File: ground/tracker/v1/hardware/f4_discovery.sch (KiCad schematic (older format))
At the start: 22 parts

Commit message: changed optimisation from Os to O3 and moved clearing of exti to just after it was read as set. Now seems to be not giving exti failed messages. So looks like its stable at the mo
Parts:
- removed C?: 0.1uF, symbol C
- removed D?: DIODE, symbol DIODE
- removed H-Bridge, P? (x2): CONN_1, symbol CONN_1
- removed P?: H-bridge GND, symbol CONN_1
- removed P?: CONN_4, symbol CONN_4
- added C1: 0.1uF, symbol C
- added C2: 1000uF, symbol CP1
- added C?: 100uF, symbol CP1
- added K2: CONN_3, symbol CONN_3
- added P2: CONN_6, symbol CONN_6
- added P5, P6, P? (x2): CONN_1, symbol CONN_1
- added P8: MAGGPS, symbol CONN_9
- added R1: 100R, symbol R
- added R10, R11, R12, R13, R14, R15, R16, R3, R4, R5, R6, R7, R8, R9: R, symbol R
- added R17, R2: 50R, symbol R
- added R? (x2): 10k, symbol R
- added SW?: SPST, symbol SPST
- added U3: BEC, symbol 7805
- added U?: 24C16, symbol 24C16
- C4: renamed from C?; value 470uF -> 10uF
- P9: renamed from P?; value CONN_5 -> RCOUT
- gave numbers to parts that had none: 13
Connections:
- net labels added: +12V, +3.3V, +6V, AV_TELEM_CDT, AV_TELEM_IN, AXMOTBV, AZ5V, AZMOT5V, AZMOTAV, AZMOTGND, AZNDIR, AZSENS, BEC5V, DiAZDIR, DiAZENCA, DiAZENCB, DiAZMOTAV, DiAZMOTBV, DiAZNDIR, DiAZPWM, DiGPSRXI, DiGPSTXO, DiMAGRDY, DiMAGSCL, DiMAGSDA, DiSLSPRXI, DiSLSPTXO, DiTSSIG, GPS5V, GPSGND, GPSRXI, GPSTXO, MAG5V, MAGGND, MAGRDY, MAGSCL, MAGSDA, RCGND, SLSPGND, SLSPRXI, SLSPTXO, TSBEC5V, TSGND, TSSIG
- net labels removed: 5VBEC, AZMOTA, AZMOTB, AZSENSE, ENC5V, ENCGND, NAZDIR, RCOUTGND, SP1RXI, SP1TXO, SPI1GND, TLTSRVOPWM
- wire segments 144 -> 329
- no-connect marks 0 -> 4
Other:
- moved on the sheet: C4, C5, C6, K1, P1, P10, P11, P12, P3, P4, P7, P9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

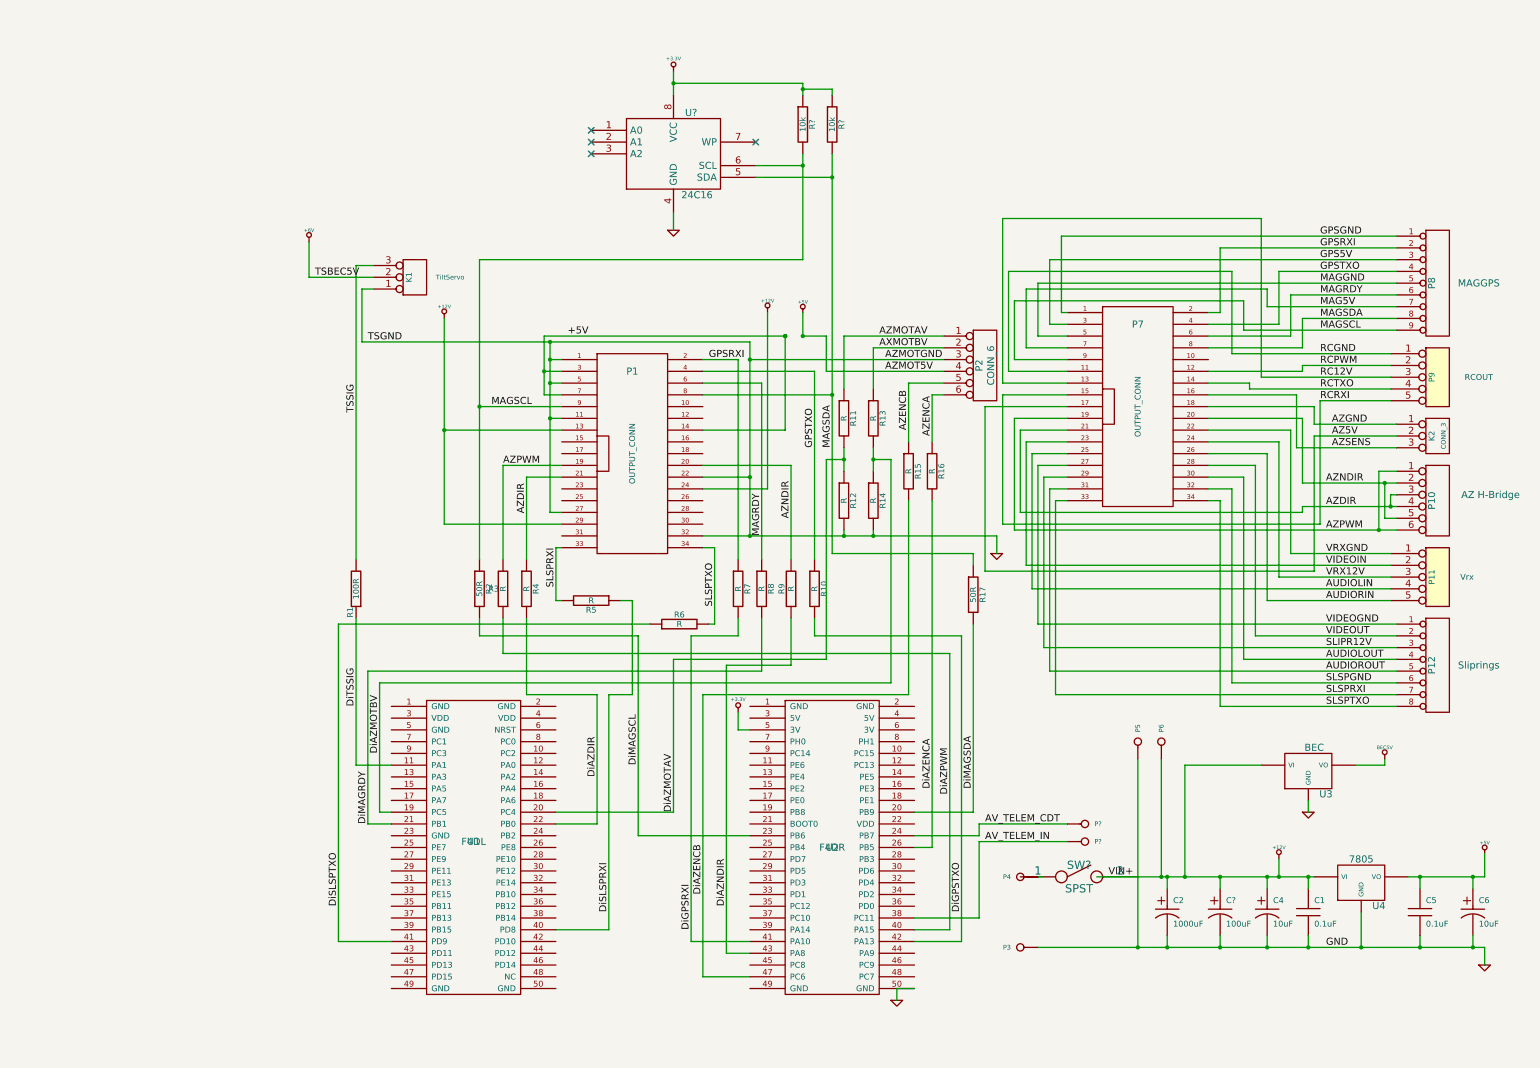
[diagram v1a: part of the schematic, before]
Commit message: prior to sorting serial port naming
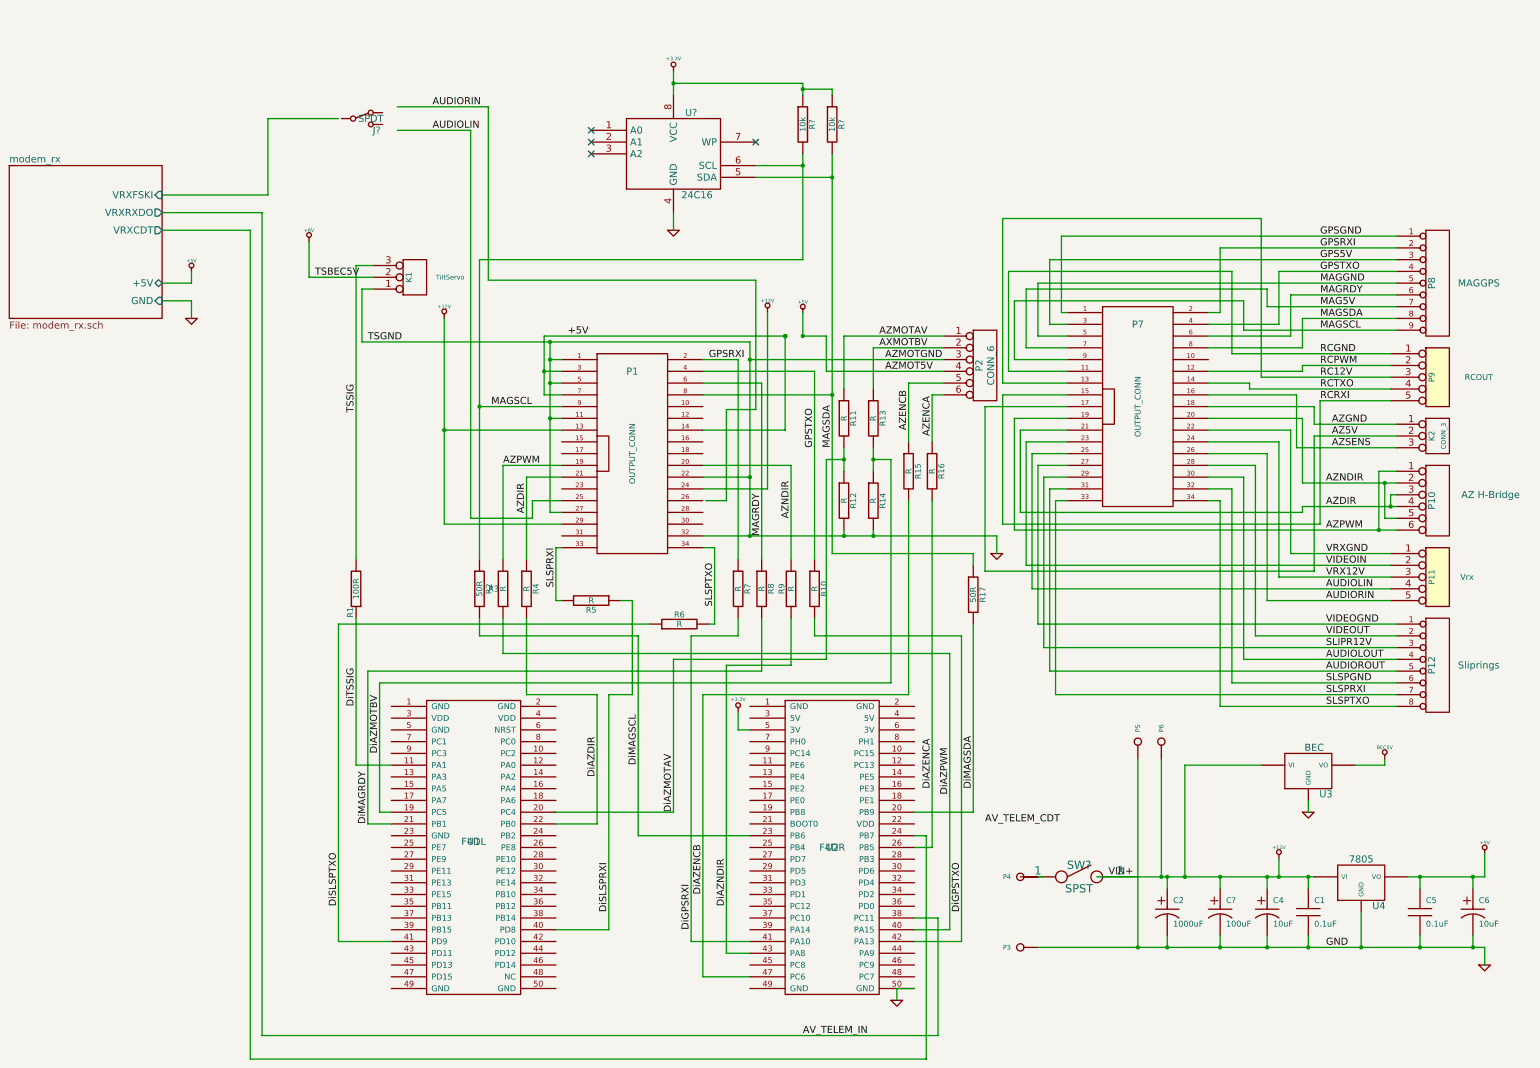
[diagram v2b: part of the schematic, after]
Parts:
- removed P? (x2): CONN_1, symbol CONN_1
- added J?: SPDT, symbol SPDT
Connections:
- net AUDIOLIN: now also P1.25 (P25)
- net AV_TELEM_CDT: no longer U2.24 (PB7)
- new net modem_rx/VRXCDT: U2.24 (PB7)

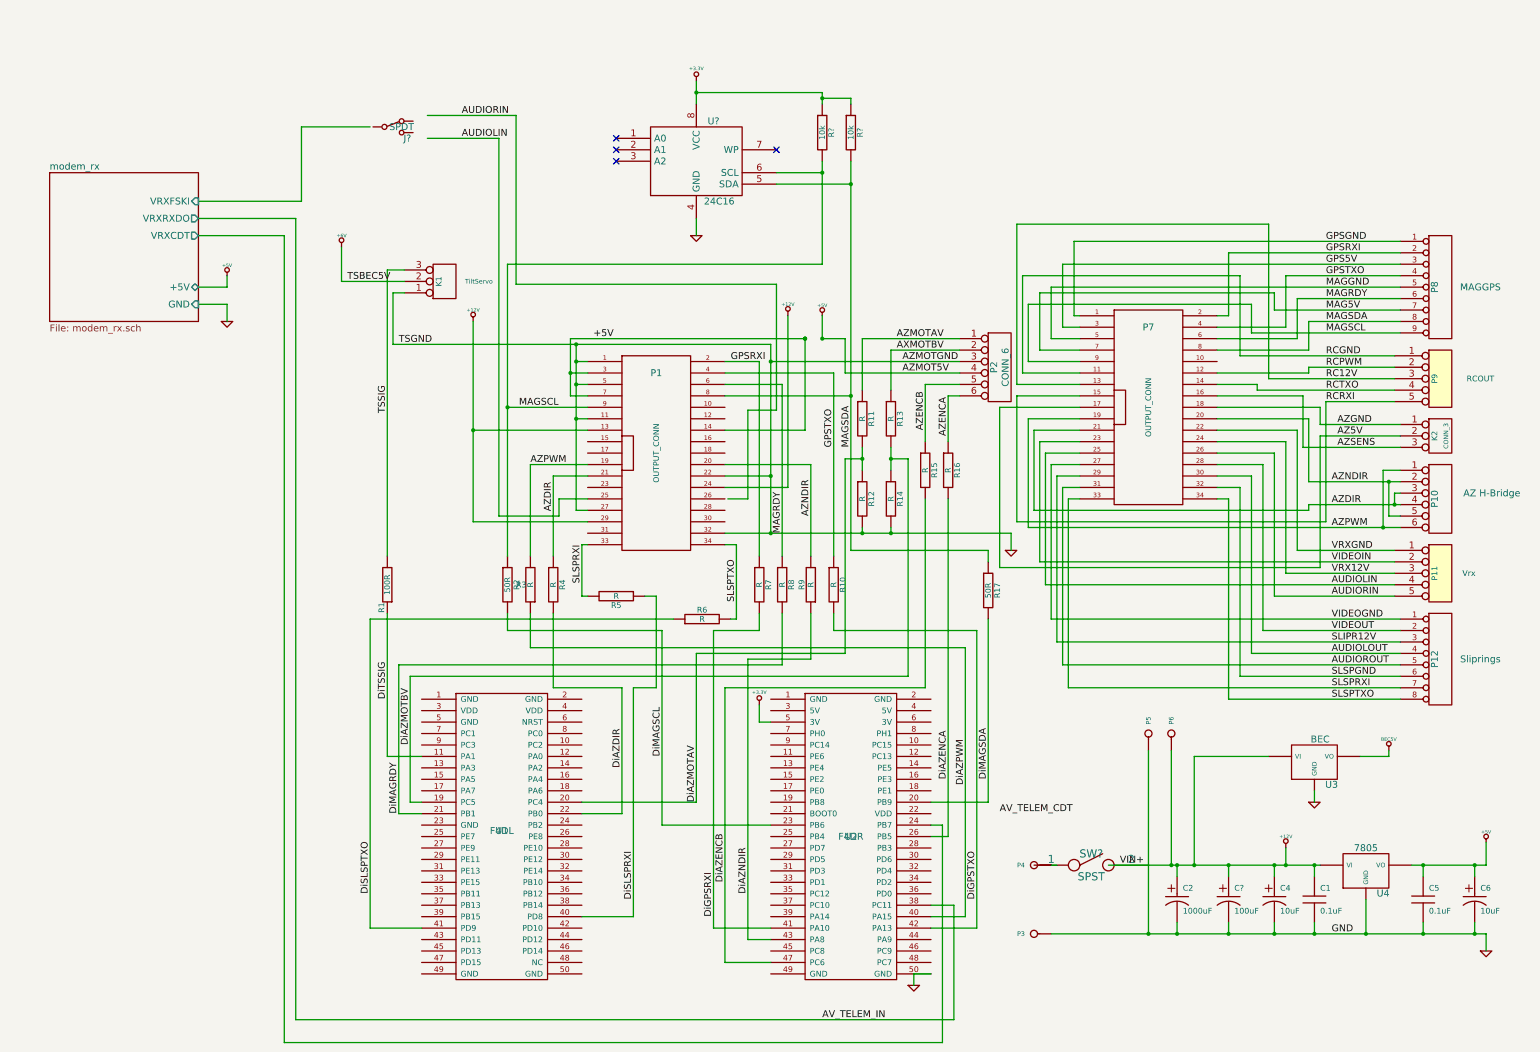
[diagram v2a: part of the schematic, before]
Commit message: incorporated digital fsk demod routine, got flashhing lights, indicating getting data, now to test if tracking.EDIT: Tested in garden, and seems to track ok so fp context appears to be saving correctly^X
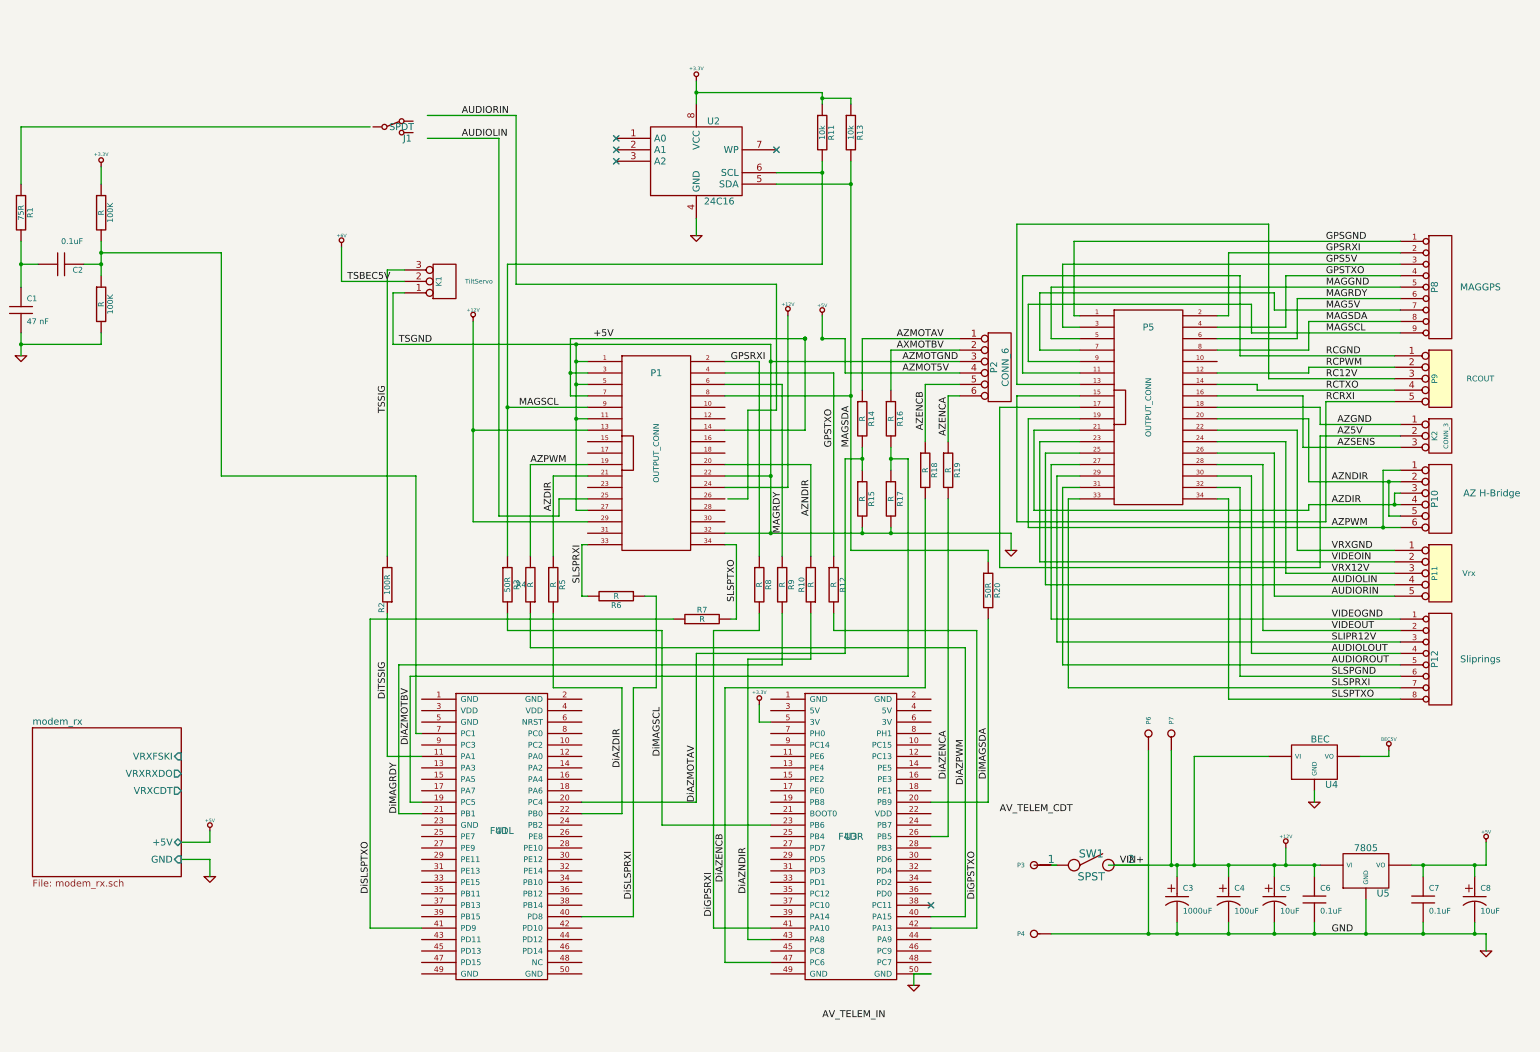
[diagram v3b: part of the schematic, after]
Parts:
- added 100K (x2): R, symbol R
- added C1: 47 nF, symbol C
- added C2: 0.1uF, symbol C
- added R1: 75R, symbol R
- gave numbers to parts that had none: 6
- renumbered C2 to C3, C4 to C5, C1 to C6, C5 to C7, C6 to C8, P4 to P3, P3 to P4, P7 to P5, P5 to P6, P6 to P7, R9 to R10, R10 to R12, R11 to R14, R12 to R15, R13 to R16, R14 to R17, R15 to R18, R16 to R19, R1 to R2, R17 to R20, R2 to R3, R3 to R4, R4 to R5, R5 to R6, R6 to R7, R7 to R8, R8 to R9, U2 to U3, U3 to U4, U4 to U5
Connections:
- net +3.3V: now also 100K.1
- net AV_TELEM_IN: no longer U3.38 (PC11)
- net GND: now also 100K.2, C1.2
- net modem_rx/VRXCDT: no longer U3.24 (PB7)
- net at U1.7 (PC1): now also 100K.1, 100K.2, C2.1
- new net: C1.1, C2.2, R1.2
- no-connect marks 4 -> 5

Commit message: prior to mod to differential fsk adc inputs
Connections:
- net at U3.24 (PB7): now also U3.38 (PC11)
- no-connect marks 5 -> 4

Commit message: got tracker v2 video working but no sp as yet
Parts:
- removed P1, P5: OUTPUT_CONN, symbol OUTPUT_CONN
- removed U1: F4DL, symbol F4DL
- removed U2: 24C16, symbol 24C16
- removed U3: F4DR, symbol F4DR
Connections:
- net labels removed: AV_TELEM_IN, DiAZDIR, DiAZENCA, DiAZENCB, DiAZMOTAV, DiAZMOTBV, DiAZNDIR, DiAZPWM, DiGPSRXI, DiGPSTXO, DiMAGRDY, DiMAGSCL, DiMAGSDA, DiSLSPRXI, DiSLSPTXO, DiTSSIG
- wire segments 318 -> 259
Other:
- note added: "Azimuth motor \nvoltage feedback"
- moved on the sheet: 100K, C1, C2, C3, C4, C5, C6, C7, C8, J1, K1, K2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
